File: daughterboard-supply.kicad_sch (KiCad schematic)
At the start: 19 parts, among them J9 39281103, SW1 1X03, U15 AP62301WU-7, U4 AP62301WU-7

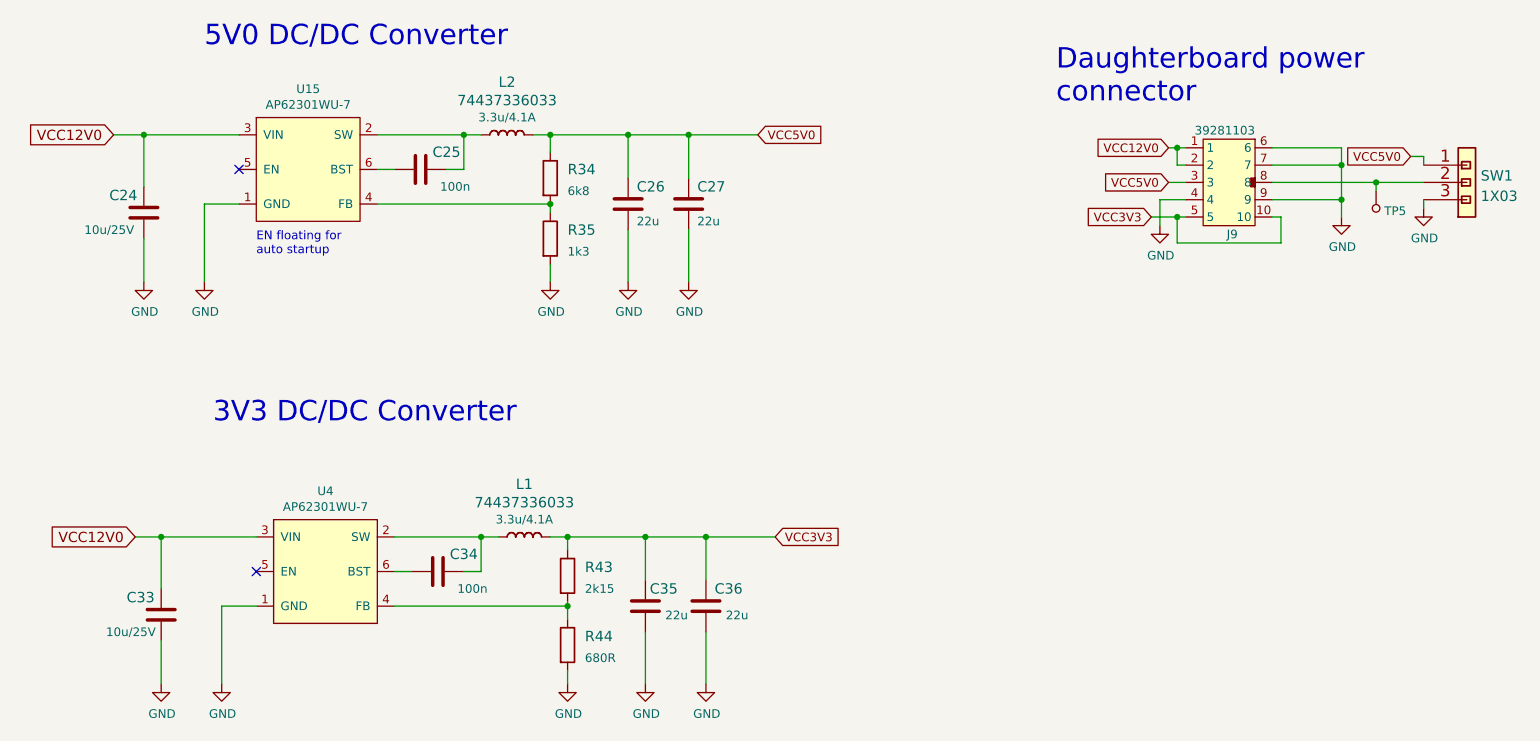
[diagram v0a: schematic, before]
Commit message: Perform globlib and find alterante components
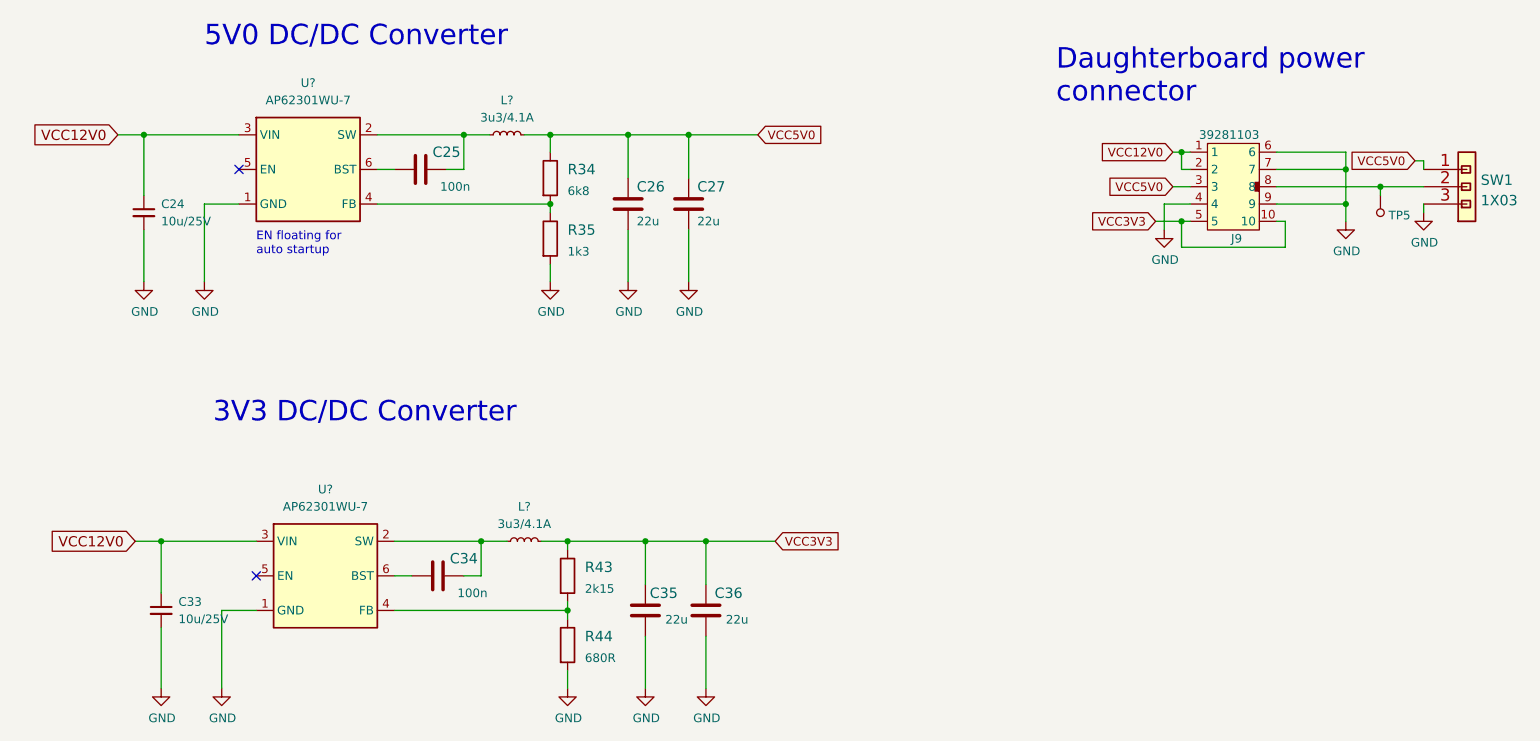
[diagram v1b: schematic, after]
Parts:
- removed C24, C33: C_10u_16V_0603, gpu-cluster-backplane-footprints:0603-cap, symbol gpu-cluster-backplane:C_10u_25V_0603
- removed L1, L2: 74437336033, gpu-cluster-backplane-footprints:WE_74437336033, symbol gpu-cluster-backplane:74437336033
- removed U15, U4: AP62301WU-7, gpu-cluster-backplane-footprints:TSOT23-6, symbol gpu-cluster-backplane:AP62301WU-7
- added C24, C33: C_10u_25V_0603, antmicro-footprints:C_0603_1608Metric, symbol antmicroCapacitors0603:C_10u_25V_0603
- added L? (x2): L_3u3_4.1A_WE-LHMI-5030, antmicro-footprints:L_WE-LHMI-5030, symbol antmicroFixedInductors:L_3u3_4.1A_WE-LHMI-5030
- added U? (x2): AP62301_TSOT, antmicro-footprints:TSOT23-6, symbol antmicroDCDCConverters:AP62301_TSOT
- C25, C34: footprint gpu-cluster-backplane-footprints:0402-cap -> antmicro-footprints:C_0402_1005Metric; symbol gpu-cluster-backplane:C_100n_0402 -> antmicroCapacitors0402:C_100n_0402
- C26, C27, C35, C36: footprint gpu-cluster-backplane-footprints:0603-cap -> antmicro-footprints:C_0603_1608Metric; symbol gpu-cluster-backplane:C_22u_0603 -> antmicroCapacitors0603:C_22u_0603
- R44: footprint antmicro-footprints:0402-res -> antmicro-footprints:R_0402_1005Metric
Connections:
- net GND: now also C24.2, C33.2, U?.1 (GND), U?.1 (GND)
- net VCC12V0: now also C24.1, C33.1, U?.3 (VIN), U?.3 (VIN)
- net VCC3V3: now also L?.2
- net VCC5V0: now also L?.2
- net at C25.1: now also L?.1, U?.2 (SW)
- net at R34.2, R35.1: now also U?.4 (FB)
- net at C25.2: now also U?.6 (BST)
- net at C34.1: now also L?.1, U?.2 (SW)
- net at R43.2, R44.1: now also U?.4 (FB)
- net at C34.2: now also U?.6 (BST)
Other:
- moved on the sheet: C34, C35, C36, J9, SW1, TP5
